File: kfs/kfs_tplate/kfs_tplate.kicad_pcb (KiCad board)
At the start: 2 copper layers, 256 x 90.6 mm, 74 parts, among them SW0 SWITCH, SW1 SWITCH, SW10 SWITCH, SW11 SWITCH, SW12 SWITCH, SW13 SWITCH, SW14 SWITCH, SW15 SWITCH, SW16 SWITCH, SW17 SWITCH, SW18 SWITCH, SW19 SWITCH, SW2 SWITCH, SW20 SWITCH, SW21 SWITCH, SW22 SWITCH, SW23 SWITCH, SW24 SWITCH, SW25 SWITCH, SW26 SWITCH, SW27 SWITCH, SW28 SWITCH, SW29 SWITCH, SW3 SWITCH, SW30 SWITCH, SW31 SWITCH, SW32 SWITCH, SW33 SWITCH, SW34 SWITCH, SW35 SWITCH, SW36 SWITCH, SW37 SWITCH, SW38 SWITCH, SW39 SWITCH, SW4 SWITCH, SW40 SWITCH, SW41 SWITCH, SW42 SWITCH, SW43 SWITCH, SW44 SWITCH, SW45 SWITCH, SW46 SWITCH, SW47 SWITCH, SW48 SWITCH, SW49 SWITCH, SW5 SWITCH, SW50 SWITCH, SW51 SWITCH, SW52 SWITCH, SW53 SWITCH, SW54 SWITCH, SW55 SWITCH, SW56 SWITCH, SW57 SWITCH, SW58 SWITCH, SW59 SWITCH, SW6 SWITCH, SW60 SWITCH, SW61 SWITCH, SW62 SWITCH, SW63 SWITCH, SW7 SWITCH, SW8 SWITCH, SW9 SWITCH

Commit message: Slight mods to kfs.
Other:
- board size 256 x 90.6 mm -> 256 x 94.5 mm
- board text added: "KEYS FOR SUCCESS"
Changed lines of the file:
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@@
     (pad "1" thru_hole circle (at 0 0) (size 3.5 3.5) (drill 2.2) (layers "*.Cu" "*.Mask"))
   )
-  (gr_arc (start 144 22.44) (mid 144.146447 22.086447) (end 144.5 21.94)
+  (gr_arc (start 268 18) (mid 270.828427 19.171573) (end 272 22)
     (stroke (width 0.1) (type default)) (layer "Edge.Cuts"))
-  (gr_line (start 125.5 21.94) (end 20 21.94)
+  (gr_arc (start 125.5 18) (mid 125.853553 18.146447) (end 126 18.5)
     (stroke (width 0.1) (type default)) (layer "Edge.Cuts"))
-  (gr_line (start 144 59) (end 144 22.44)
+  (gr_arc (start 144 18.5) (mid 144.146447 18.146447) (end 144.5 18)
     (stroke (width 0.1) (type default)) (layer "Edge.Cuts"))
-  (gr_arc (start 16 25.94) (mid 17.171573 23.111573) (end 20 21.94)
+  (gr_line (start 125.5 18) (end 20 18)
     (stroke (width 0.1) (type default)) (layer "Edge.Cuts"))
-  (gr_line (start 126.5 59.5) (end 143.5 59.5)
+  (gr_line (start 144.5 18) (end 268 18)
+    (stroke (width 0.1) (type default)) (layer "Edge.Cuts"))
+  (gr_line (start 144 54.75) (end 144 18.5)
     (stroke (width 0.1) (type default)) (layer "Edge.Cuts"))
   (gr_arc (start 20 112.5) (mid 17.171573 111.328427) (end 16 108.5)
     (stroke (width 0.1) (type default)) (layer "Edge.Cuts"))
-  (gr_line (start 144.5 21.94) (end 268 21.94)
-    (stroke (width 0.1) (type default)) (layer "Edge.Cuts"))
-  (gr_arc (start 268 21.94) (mid 270.828427 23.111573) (end 272 25.94)
+  (gr_arc (start 144 54.75) (mid 143.853553 55.103553) (end 143.5 55.25)
     (stroke (width 0.1) (type default)) (layer "Edge.Cuts"))
   (gr_arc (start 272 108.5) (mid 270.828427 111.328427) (end 268 112.5)
     (stroke (width 0.1) (type default)) (layer "Edge.Cuts"))
-  (gr_arc (start 126.5 59.5) (mid 126.146447 59.353553) (end 126 59)
+  (gr_arc (start 126.5 55.25) (mid 126.146447 55.103553) (end 126 54.75)
     (stroke (width 0.1) (type default)) (layer "Edge.Cuts"))
-  (gr_arc (start 144 59) (mid 143.853553 59.353553) (end 143.5 59.5)
+  (gr_arc (start 16 22) (mid 17.171573 19.171573) (end 20 18)
     (stroke (width 0.1) (type default)) (layer "Edge.Cuts"))
-  (gr_line (start 126 22.44) (end 126 59)
-    (stroke (width 0.1) (type default)) (layer "Edge.Cuts"))
-  (gr_arc (start 125.5 21.94) (mid 125.853553 22.086447) (end 126 22.44)
-    (stroke (width 0.1) (type default)) (layer "Edge.Cuts"))
-  (gr_line (start 16 25.94) (end 16 108.5)
+  (gr_line (start 16 22) (end 16 108.5)
     (stroke (width 0.1) (type default)) (layer "Edge.Cuts"))
   (gr_line (start 20 112.5) (end 268 112.5)
     (stroke (width 0.1) (type default)) (layer "Edge.Cuts"))
-  (gr_line (start 272 108.5) (end 272 25.94)
+  (gr_line (start 126 18.5) (end 126 54.75)
     (stroke (width 0.1) (type default)) (layer "Edge.Cuts"))
+  (gr_line (start 272 108.5) (end 272 22)
+    (stroke (width 0.1) (type default)) (layer "Edge.Cuts"))
+  (gr_line (start 126.5 55.25) (end 143.5 55.25)
+    (stroke (width 0.1) (type default)) (layer "Edge.Cuts"))
+  (gr_text "KEYS FOR SUCCESS" (at 162 24.5) (layer "F.SilkS")
+    (effects (font (size 4 4) (thickness 0.5)) (justify left bottom))
+  )
 )

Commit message: Moved some mounting holes on the kfs.
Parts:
- moved H0 23.2 mm to (148.0, 24.0)
- moved H4 23.2 mm to (122.0, 24.0)
- moved H3 17.0 mm to (216.0, 59.5)
- moved H7 14.1 mm to (22.0, 24.0)
- moved H9 14.1 mm to (266.0, 24.0)
- moved H10 4.53 mm to (266.0, 106.5)
- moved H8 4.53 mm to (22.0, 106.5)
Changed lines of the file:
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@@
   )
   (footprint "MountingHole:MountingHole_2.2mm_M2_ISO7380_Pad" (layer "F.Cu")
-    (at 162 42.5)
+    (at 148 24)
     (descr "Mounting Hole 2.2mm, M2, ISO7380")
     (tags "mounting hole 2.2mm m2 iso7380")
@@
   )
   (footprint "MountingHole:MountingHole_2.2mm_M2_ISO7380_Pad" (layer "F.Cu")
-    (at 265.5 102)
+    (at 266 106.5)
     (descr "Mounting Hole 2.2mm, M2, ISO7380")
     (tags "mounting hole 2.2mm m2 iso7380")
@@
   )
   (footprint "MountingHole:MountingHole_2.2mm_M2_ISO7380_Pad" (layer "F.Cu")
-    (at 22.5 102)
+    (at 22 106.5)
     (descr "Mounting Hole 2.2mm, M2, ISO7380")
     (tags "mounting hole 2.2mm m2 iso7380")
@@
   )
   (footprint "MountingHole:MountingHole_2.2mm_M2_ISO7380_Pad" (layer "F.Cu")
-    (at 36 25.5)
+    (at 22 24)
     (descr "Mounting Hole 2.2mm, M2, ISO7380")
     (tags "mounting hole 2.2mm m2 iso7380")
@@
   )
   (footprint "MountingHole:MountingHole_2.2mm_M2_ISO7380_Pad" (layer "F.Cu")
-    (at 108 42.5)
+    (at 122 24)
     (descr "Mounting Hole 2.2mm, M2, ISO7380")
     (tags "mounting hole 2.2mm m2 iso7380")
@@
   )
   (footprint "MountingHole:MountingHole_2.2mm_M2_ISO7380_Pad" (layer "F.Cu")
-    (at 216 76.5)
+    (at 216 59.5)
     (descr "Mounting Hole 2.2mm, M2, ISO7380")
     (tags "mounting hole 2.2mm m2 iso7380")
@@
   )
   (footprint "MountingHole:MountingHole_2.2mm_M2_ISO7380_Pad" (layer "F.Cu")
-    (at 252 25.5)
+    (at 266 24)
     (descr "Mounting Hole 2.2mm, M2, ISO7380")
     (tags "mounting hole 2.2mm m2 iso7380")

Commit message: Switched to staggered kfs layout.
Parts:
- moved H3 200.3 mm to (16.5, 41.5)
- moved H8 196.2 mm to (216.0, 77.0)
- moved H5 184.1 mm to (289.5, 124.5)
- moved H10 150.7 mm to (130.0, 41.5)
- moved H2 137.7 mm to (289.5, 41.5)
- moved H4 114.1 mm to (176.0, 124.5)
- moved H9 109.4 mm to (158.0, 41.5)
- moved H0 106.8 mm to (112.0, 124.5)
- moved H6 85.5 mm to (16.5, 124.5)
- moved H7 72.9 mm to (72.0, 77.0)
- moved SW43 31.9 mm to (202.5, 119.0)
- moved SW48 31.9 mm to (225.0, 119.0)
- moved SW53 31.9 mm to (243.0, 119.0)
- moved SW58 31.9 mm to (261.0, 119.0)
- moved SW63 31.9 mm to (279.0, 119.0)
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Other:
- board size 256 x 94.5 mm -> 283 x 93 mm

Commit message: Moved the bottom row of kfs farther inward.
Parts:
- added H1: MountingHole, MountingHole:MountingHole_2.2mm_M2_ISO7380_Pad, F.Cu at (153.0, 93.5)
- moved SW14 9.00 mm to (72.0, 119.0)
- moved SW19 9.00 mm to (94.5, 119.0)
- moved SW4 9.00 mm to (36.0, 119.0)
- moved SW43 9.00 mm to (193.5, 119.0)
- moved SW48 9.00 mm to (216.0, 119.0)
- moved SW53 9.00 mm to (234.0, 119.0)
- moved SW58 9.00 mm to (252.0, 119.0)
- moved SW63 9.00 mm to (270.0, 119.0)
- moved SW9 9.00 mm to (54.0, 119.0)

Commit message: Updated reset button and mounting holes on kfs.
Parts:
- removed H1, H7, H8: MountingHole, MountingHole:MountingHole_2.2mm_M2_ISO7380_Pad

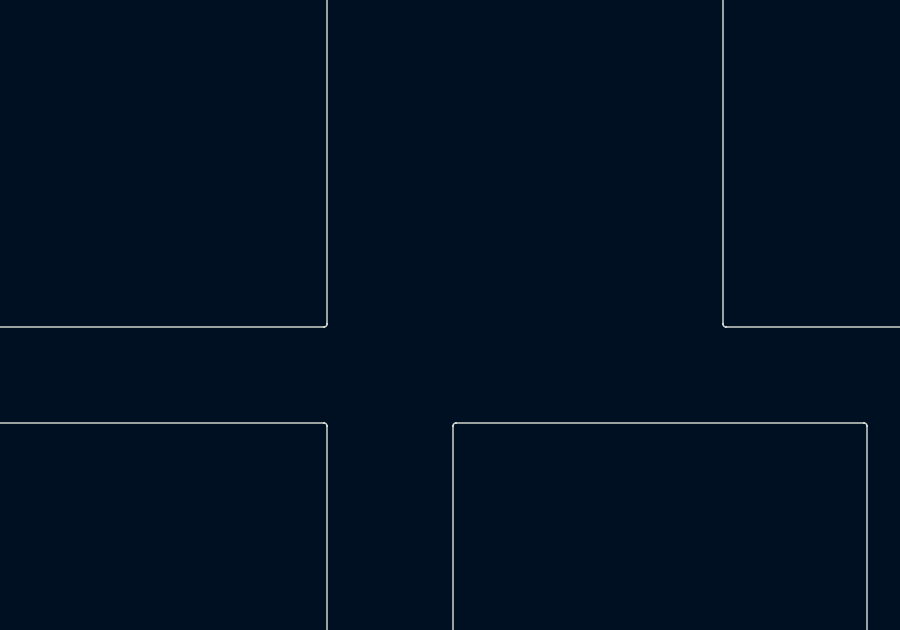
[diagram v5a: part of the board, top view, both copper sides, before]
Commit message: Changed reset button again. Removed some standoffs.
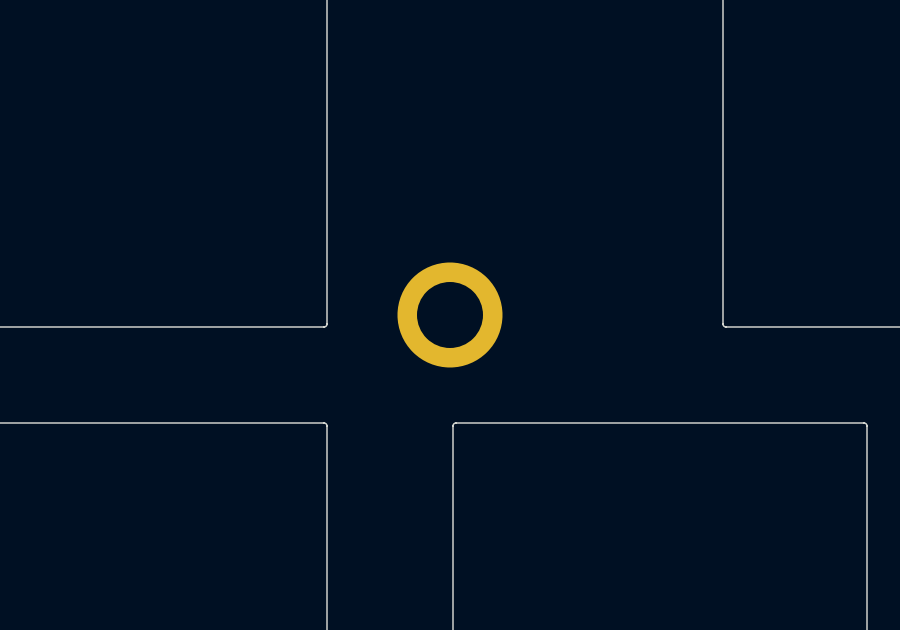
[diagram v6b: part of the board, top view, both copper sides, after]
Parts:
- added H1: MountingHole, MountingHole:MountingHole_2.2mm_M2_ISO7380_Pad, F.Cu at (155.0, 91.5)
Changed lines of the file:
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@@
       (stroke (width 0.05) (type default)) (layer "Edge.Cuts"))
+  )
+  (footprint "MountingHole:MountingHole_2.2mm_M2_ISO7380_Pad" (layer "F.Cu")
+    (at 155 91.5)
+    (descr "Mounting Hole 2.2mm, M2, ISO7380")
+    (tags "mounting hole 2.2mm m2 iso7380")
+    (property "Sheetfile" "kfs_tplate.kicad_sch")
+    (property "Sheetname" "")
+    (property "ki_description" "Mounting Hole without connection")
+    (property "ki_keywords" "mounting hole")
+    (attr exclude_from_pos_files)
+    (fp_text reference "H1" (at 0 -2.75) (layer "F.SilkS") hide
+        (effects (font (size 1 1) (thickness 0.15)))
+    )
+    (fp_text value "MountingHole" (at 0 2.75) (layer "F.Fab")
+        (effects (font (size 1 1) (thickness 0.15)))
+    )
+    (fp_text user "${REFERENCE}" (at 0 0) (layer "F.Fab")
+        (effects (font (size 1 1) (thickness 0.15)))
+    )
+    (fp_circle (center 0 0) (end 1.75 0)
+      (stroke (width 0.15) (type solid)) (fill none) (layer "Cmts.User"))
+    (fp_circle (center 0 0) (end 2 0)
+      (stroke (width 0.05) (type solid)) (fill none) (layer "F.CrtYd"))
+    (pad "1" thru_hole circle (at 0 0) (size 3.5 3.5) (drill 2.2) (layers "*.Cu" "*.Mask"))
   )
   (footprint "footprints:kailh_choc_plate" (layer "F.Cu")

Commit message: Switched kfs to use nice!nano.
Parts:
- added H11: MountingHole, MountingHole:MountingHole_2.2mm_M2_ISO7380_Pad, F.Cu at (298.5, 76.5)
- added H7: MountingHole, MountingHole:MountingHole_2.2mm_M2_ISO7380_Pad, F.Cu at (139.5, 83.0)
- added H8: MountingHole, MountingHole:MountingHole_2.2mm_M2_ISO7380_Pad, F.Cu at (25.5, 76.5)
- moved H1 14.3 mm to (166.5, 83.0)
- moved H0 12.4 mm to (121.0, 116.0)
- moved H4 12.4 mm to (185.0, 116.0)
- moved H5 12.4 mm to (298.5, 116.0)
- moved H6 12.4 mm to (25.5, 116.0)
- moved SW0 12.4 mm to (45.0, 42.5)
- moved SW1 12.4 mm to (40.5, 59.5)
- moved SW10 12.4 mm to (81.0, 42.5)
- moved SW11 12.4 mm to (76.5, 59.5)
- moved SW12 12.4 mm to (72.0, 76.5)
- moved SW13 12.4 mm to (67.5, 93.5)
- moved SW14 12.4 mm to (81.0, 110.5)
- moved SW15 12.4 mm to (99.0, 42.5)
- moved SW16 12.4 mm to (94.5, 59.5)
- moved SW17 12.4 mm to (90.0, 76.5)
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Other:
- board size 283 x 93 mm -> 283 x 95.5 mm
- board text added: "CHRISTINE IS CUTE!"

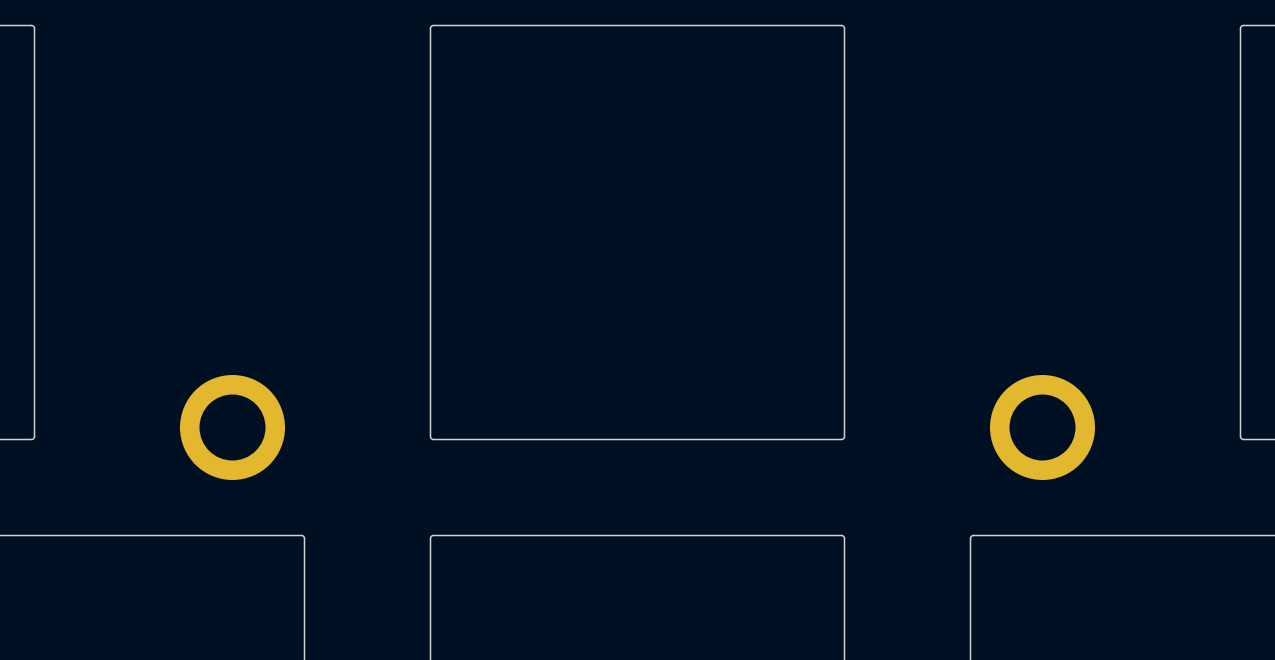
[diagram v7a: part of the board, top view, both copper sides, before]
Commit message: Moved some kfs mounting holes.
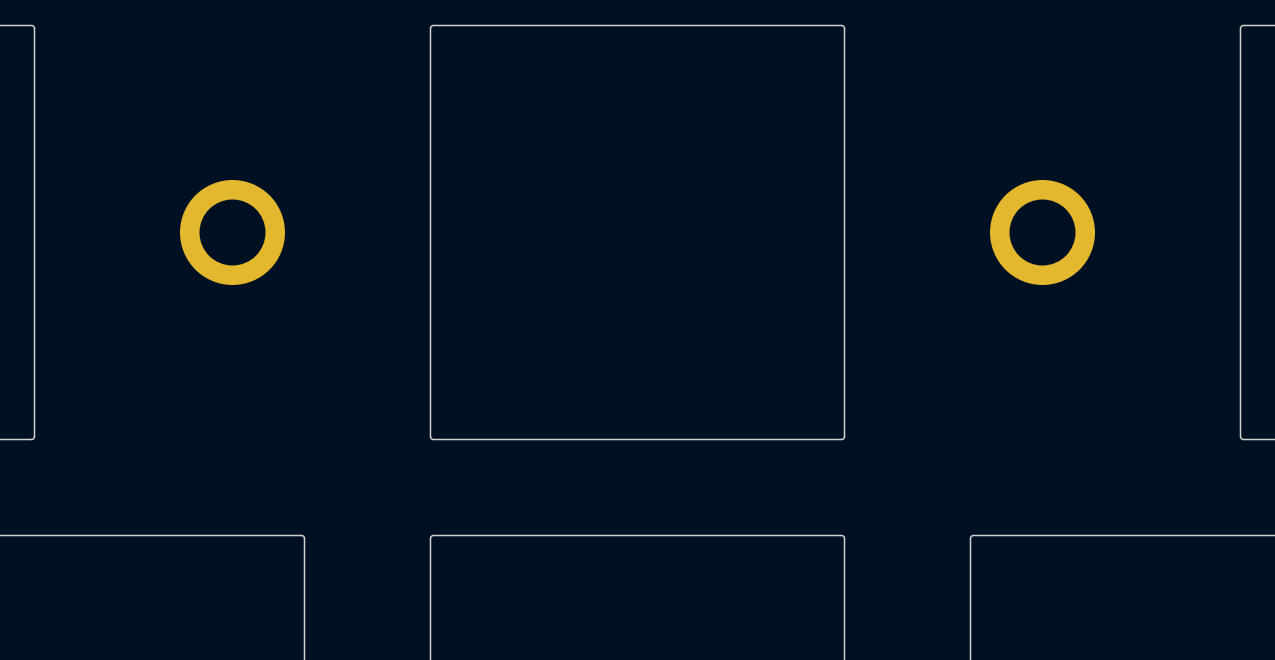
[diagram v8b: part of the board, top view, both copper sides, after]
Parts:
- moved H1 6.50 mm to (166.5, 76.5)
- moved H7 6.50 mm to (139.5, 76.5)
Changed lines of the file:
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@@
   )
   (footprint "MountingHole:MountingHole_2.2mm_M2_ISO7380_Pad" (layer "F.Cu")
-    (at 166.5 83)
+    (at 166.5 76.5)
     (descr "Mounting Hole 2.2mm, M2, ISO7380")
     (tags "mounting hole 2.2mm m2 iso7380")
@@
   )
   (footprint "MountingHole:MountingHole_2.2mm_M2_ISO7380_Pad" (layer "F.Cu")
-    (at 139.5 83)
+    (at 139.5 76.5)
     (descr "Mounting Hole 2.2mm, M2, ISO7380")
     (tags "mounting hole 2.2mm m2 iso7380")
